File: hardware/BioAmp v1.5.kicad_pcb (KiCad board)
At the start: 2 copper layers, 32 x 60 mm, 34 parts, among them J1 Conn_01x02_Male, J2 PJ-3062-CO, J4 Conn_01x03_Male, J5 Conn_01x02_Male, J6 Conn_01x02_Male, J7 Conn_01x02_Male, U1 TL074

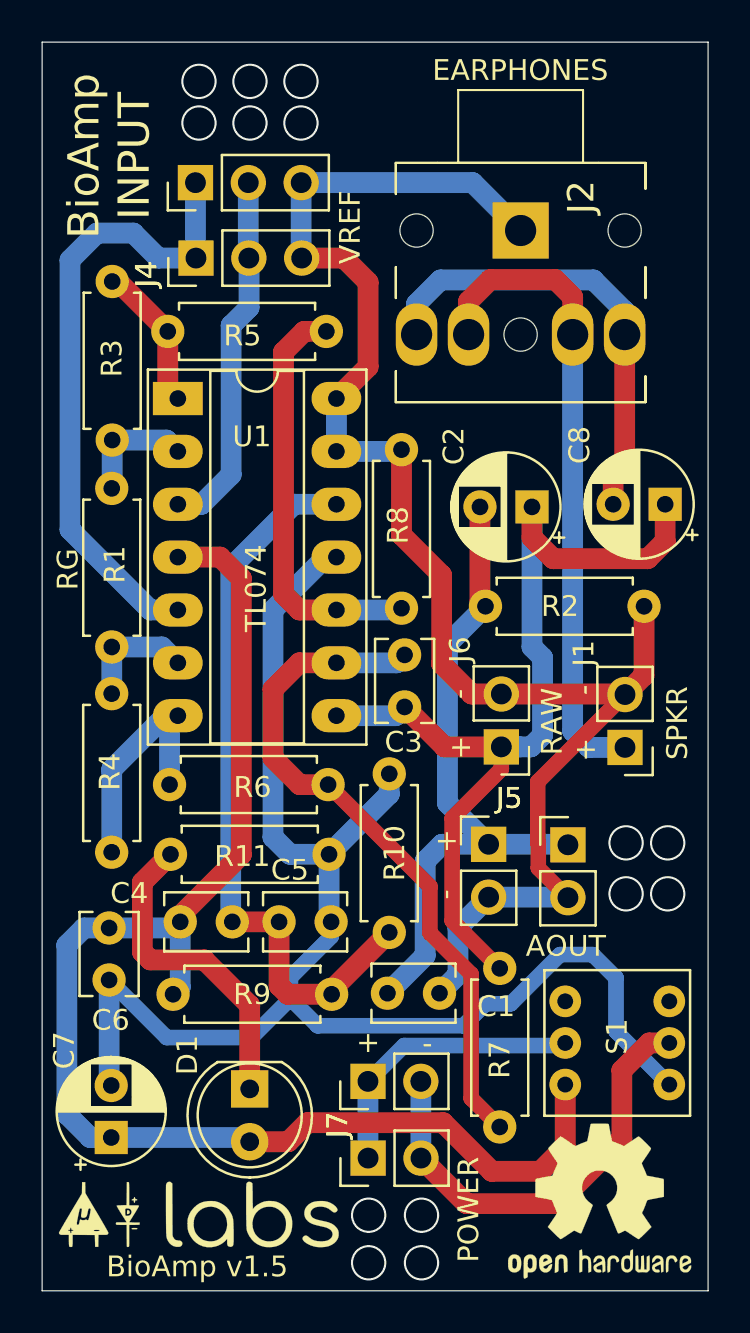
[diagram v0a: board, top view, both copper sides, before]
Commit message: BioAmp v1.5.7 hardware files
Small modification for the holes in this update.
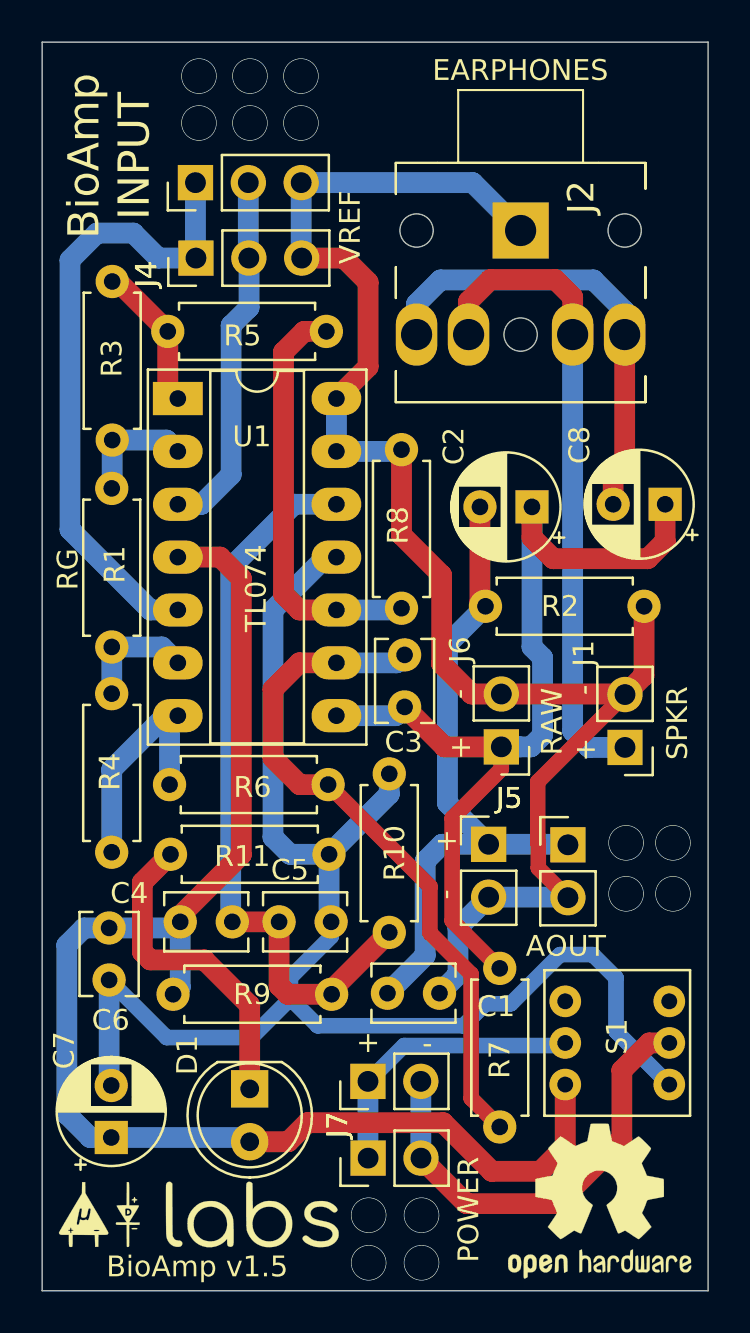
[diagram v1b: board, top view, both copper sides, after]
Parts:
- C1, C3: value 4.7nf -> 100nF
- C2, C7, C8: value CP -> 47uF
- C4, C5, C6: value 100nf -> 100nF
- J4: value Conn_01x03_Male -> Electode cable
- J5: value Conn_01x02_Male -> Audio cable
- J7: value Conn_01x02_Male -> 9v snap
- renumbered G*** to REF**
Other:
- board text added: "Rev 1.5.7"
- board text removed: "Rev 1.5.6"
